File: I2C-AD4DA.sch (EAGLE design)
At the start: 11 parts, among them IC1 PCF8591T, X1 RJ45-FRONT

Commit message: 1.1
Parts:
- added CA, CB, CC, CD: 0.1uF, SPCoast:CAP0805
- added L1: 47 uH, rcl:L-USL2012C
- added U$1: AGND+DGND, SPCoast:AGND+DGND
- C1: device SPCoast-minimal:C-POL0810 -> SPCoast:CAP-POLUD10X10
- C2: device SPCoast-minimal:C0805 -> SPCoast:CAP0805
- I2C0, I2C1: value I2CLEFT -> CONNECTOR-I2CLEFT; device SPCoast-minimal:I2CLEFT -> SPCoast:CONNECTOR-I2CLEFT
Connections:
- new net N$1: IC1.VREF, L1.2
- net 5V: now also L1.1
- net AD0: now also CA.1
- net AD1: now also CB.1
- net AD2: now also CC.1
- net AD3: now also CD.1
- net AGND: now also CA.2, CB.2, CC.2, CD.2, IC1.AGND, U$1.P$1
- net GND: now also U$1.P$2; no longer IC1.AGND
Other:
- note added: "1.1"
- note removed: "1.0"
- moved on the sheet: A0, A1, A2, I2C0, I2C1, X1

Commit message: 2.0
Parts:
- removed U$9: BOARD50X50, SPCoast-minimal:BOARD50X50
- added BOARD1: (no value), SPCoast:BOARD80X50
- added CON1, CON2: CONNECTOR-GROVE-4P-2.0-3470130P1, SPCoast:CONNECTOR-GROVE-4P-2.0-3470130P1
- A0, A1, A2: device SPCoast-minimal:JUMPER-3-DEFAULT2.54MM -> SPCoast:JUMPER-3-DEFAULT2.54MM
- IC1: device micro-philips:PCF8591T -> SPCoast:PCF8591T
- L1: device rcl:L-USL2012C -> SPCoast:L-USL2012C
- LOGO1: value OSHW-LOGOL -> DOC-OSHW-LOGO-L; device SPCoast-minimal:OSHW-LOGOL -> SPCoast:DOC-OSHW-LOGO-L
- X1: value RJ45-FRONT -> (none); device SPCoast-minimal:RJ45-FRONT -> SPCoast:CONNECTOR-RJ45-FRONT
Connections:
- new net VIN: CON1.3, CON1.4, CON2.3, CON2.4
- net GND: now also CON1.1, CON1.2, CON2.1, CON2.2
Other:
- note added: "2.0"
- note removed: "1.1"

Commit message: 3.0
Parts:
- removed X1: (no value), SPCoast:CONNECTOR-RJ45-FRONT
- added C3, C4: 0.1uF, SPCoast:CAP0805
- added U$2, U$3, U$4, U$7: R-SLIDE-POT-45MM, SPCoast:R-SLIDE-POT-45MM
- A0, A1, A2: device SPCoast:JUMPER-3-DEFAULT2.54MM -> SPCoast:JUMPER-31-2
- BOARD1: device SPCoast:BOARD80X50 -> SPCoast:BOARD80X100
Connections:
- net 5V: now also C3.1, C4.1, U$2P1.E, U$3P1.E, U$4P1.E, U$7P1.E; no longer X1.1
- net AD0: now also U$7P1.S; no longer X1.2
- net AD1: now also U$4P1.S; no longer X1.3
- net AD2: now also U$3P1.S; no longer X1.4
- net AD3: now also U$2P1.S; no longer X1.5
- net AGND: now also C3.2, U$2G$1.AGND, U$2P1.A, U$3G$1.AGND, U$3P1.A, U$4G$1.AGND, U$4P1.A, U$7G$1.AGND, U$7P1.A; no longer X1.6
- net DA0: no longer X1.7
- net GND: now also C4.2; no longer X1.8
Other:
- note added: "1.0"
- note added: "3.0"
- note added: "4x slider pots for controlling light strips"
- note added: "D"
- note added: "Update: Fixed library footprint for sliders removed extra caps analog output to a pin set, not LED"
- note removed: "2.0"

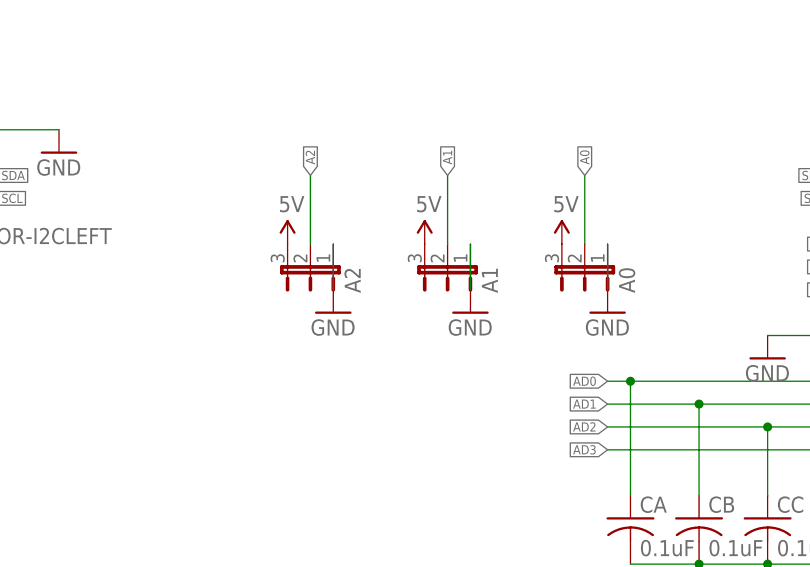
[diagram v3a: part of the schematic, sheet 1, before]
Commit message: added values for connectors
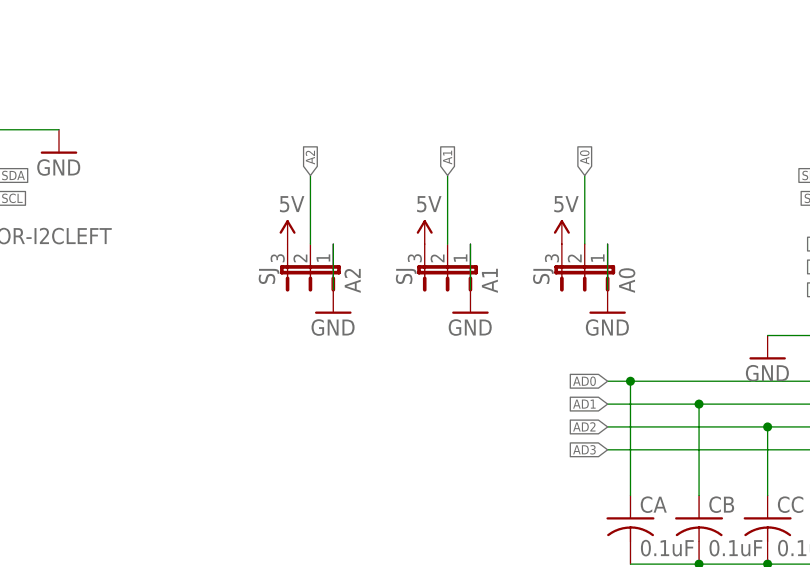
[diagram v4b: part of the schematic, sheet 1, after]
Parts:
- A0, A1, A2: value (none) -> SJ
- BOARD1: value (none) -> 10x10
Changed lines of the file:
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@@
 <part name="GND1" library="SparkFun-Aesthetics" deviceset="GND" device=""/>
 <part name="GND6" library="SparkFun-Aesthetics" deviceset="GND" device=""/>
-<part name="A2" library="SPCoast" deviceset="JUMPER-3" device="1-2"/>
-<part name="A1" library="SPCoast" deviceset="JUMPER-3" device="1-2"/>
-<part name="A0" library="SPCoast" deviceset="JUMPER-3" device="1-2"/>
+<part name="A2" library="SPCoast" deviceset="JUMPER-3" device="1-2" value="SJ"/>
+<part name="A1" library="SPCoast" deviceset="JUMPER-3" device="1-2" value="SJ"/>
+<part name="A0" library="SPCoast" deviceset="JUMPER-3" device="1-2" value="SJ"/>
 <part name="GND7" library="SparkFun-Aesthetics" deviceset="GND" device=""/>
 <part name="L1" library="SPCoast" deviceset="L-US" device="L2012C" value="47 uH"/>
@@
 <part name="U$1" library="SPCoast" deviceset="AGND+DGND" device=""/>
 <part name="GND4" library="SparkFun-Aesthetics" deviceset="GND" device=""/>
-<part name="BOARD1" library="SPCoast" deviceset="BOARD" device="80X100"/>
+<part name="BOARD1" library="SPCoast" deviceset="BOARD" device="80X100" value="10x10"/>
 <part name="CON1" library="SPCoast" deviceset="CONNECTOR-GROVE-4P-2.0" device="-3470130P1"/>
 <part name="CON2" library="SPCoast" deviceset="CONNECTOR-GROVE-4P-2.0" device="-3470130P1"/>

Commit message: normalized values
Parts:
- BOARD1: value 10x10 -> BOARD
- C1: value 150uF -> 220uF; device SPCoast:CAP-POLUD10X10 -> SPCoast:CAP-POL0810
- CON1, CON2: value CONNECTOR-GROVE-4P-2.0-3470130P1 -> 2mm
- I2C0, I2C1: value CONNECTOR-I2CLEFT -> I2C
- LOGO1: value DOC-OSHW-LOGO-L -> OSHW
- U$3, U$4, U$7: value R-SLIDE-POT-45MM -> (none)
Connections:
- net 5V: now also U$2RS1.E, U$3RS1.E, U$4RS1.E, U$7RS1.E; no longer U$2P1.E, U$3P1.E, U$4P1.E, U$7P1.E
- net AD0: now also U$7RS1.S; no longer U$7P1.S
- net AD1: now also U$4RS1.S; no longer U$4P1.S
- net AD2: now also U$3RS1.S; no longer U$3P1.S
- net AD3: now also U$2RS1.S; no longer U$2P1.S
- net AGND: now also U$2G1.AGND, U$2RS1.A, U$3G1.AGND, U$3RS1.A, U$4G1.AGND, U$4RS1.A, U$7G1.AGND, U$7RS1.A; no longer U$2G$1.AGND, U$2P1.A, U$3G$1.AGND, U$3P1.A, U$4G$1.AGND, U$4P1.A, U$7G$1.AGND, U$7P1.A
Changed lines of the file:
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@@
 <part name="GND3" library="SparkFun-Aesthetics" deviceset="GND" device=""/>
 <part name="SUPPLY1" library="SparkFun-Aesthetics" deviceset="5V" device=""/>
-<part name="C1" library="SPCoast" deviceset="CAP-POL*" device="UD10X10" value="150uF"/>
+<part name="C1" library="SPCoast" deviceset="CAP-POL*" device="0810" value="220uF"/>
 <part name="SUPPLY13" library="SparkFun-Aesthetics" deviceset="5V" device=""/>
 <part name="GND15" library="SparkFun-Aesthetics" deviceset="GND" device=""/>
 <part name="IC1" library="SPCoast" deviceset="PCF8591" device="T"/>
-<part name="I2C1" library="SPCoast" deviceset="CONNECTOR-I2C" device="LEFT"/>
-<part name="I2C0" library="SPCoast" deviceset="CONNECTOR-I2C" device="LEFT"/>
+<part name="I2C1" library="SPCoast" deviceset="CONNECTOR-I2C" device="LEFT" value="I2C"/>
+<part name="I2C0" library="SPCoast" deviceset="CONNECTOR-I2C" device="LEFT" value="I2C"/>
 <part name="SUPPLY2" library="SparkFun-Aesthetics" deviceset="5V" device=""/>
 <part name="GND1" library="SparkFun-Aesthetics" deviceset="GND" device=""/>
@@
 <part name="GND7" library="SparkFun-Aesthetics" deviceset="GND" device=""/>
 <part name="L1" library="SPCoast" deviceset="L-US" device="L2012C" value="47 uH"/>
-<part name="LOGO1" library="SPCoast" deviceset="DOC-OSHW-LOGO-" device="L" value="DOC-OSHW-LOGO-L"/>
+<part name="LOGO1" library="SPCoast" deviceset="DOC-OSHW-LOGO-" device="L" value="OSHW"/>
 <part name="C2" library="SPCoast" deviceset="CAP*" device="0805" value="0.1uF"/>
 <part name="CC" library="SPCoast" deviceset="CAP*" device="0805" value="0.1uF"/>
@@
 <part name="U$1" library="SPCoast" deviceset="AGND+DGND" device=""/>
 <part name="GND4" library="SparkFun-Aesthetics" deviceset="GND" device=""/>
-<part name="BOARD1" library="SPCoast" deviceset="BOARD" device="80X100" value="10x10"/>
-<part name="CON1" library="SPCoast" deviceset="CONNECTOR-GROVE-4P-2.0" device="-3470130P1"/>
-<part name="CON2" library="SPCoast" deviceset="CONNECTOR-GROVE-4P-2.0" device="-3470130P1"/>
+<part name="BOARD1" library="SPCoast" deviceset="BOARD" device="80X100" value="BOARD"/>
+<part name="CON1" library="SPCoast" deviceset="CONNECTOR-GROVE-4P-2.0" device="-3470130P1" value="2mm"/>
+<part name="CON2" library="SPCoast" deviceset="CONNECTOR-GROVE-4P-2.0" device="-3470130P1" value="2mm"/>
 <part name="GND8" library="SparkFun-Aesthetics" deviceset="GND" device=""/>
 <part name="FRAME2" library="SPCoast-minimal" deviceset="FRAME-LETTER" device=""/>
@@
 <instance part="GND1" gate="1" x="66.04" y="119.38"/>
 <instance part="GND6" gate="1" x="144.78" y="96.52"/>
-<instance part="A2" gate="G$1" x="96.52" y="106.68" rot="R180"/>
-<instance part="A1" gate="G$1" x="111.76" y="106.68" rot="R180"/>
-<instance part="A0" gate="G$1" x="127" y="106.68" rot="R180"/>
+<instance part="A2" gate="J" x="96.52" y="106.68" rot="R180"/>
+<instance part="A1" gate="J" x="111.76" y="106.68" rot="R180"/>
+<instance part="A0" gate="J" x="127" y="106.68" rot="R180"/>
 <instance part="GND7" gate="1" x="96.52" y="101.6"/>
 <instance part="L1" gate="G$1" x="180.34" y="111.76"/>
@@
 <instance part="U$1" gate="G$1" x="165.1" y="73.66"/>
 <instance part="GND4" gate="1" x="170.18" y="71.12"/>
-<instance part="BOARD1" gate="G$1" x="238.76" y="33.02"/>
+<instance part="BOARD1" gate="B" x="238.76" y="33.02"/>
 <instance part="CON1" gate="J" x="33.02" y="147.32"/>
 <instance part="CON2" gate="J" x="48.26" y="147.32" rot="MR0"/>
@@
 <wire x1="124.46" y1="109.22" x2="124.46" y2="116.84" width="0.1524" layer="91"/>
 <label x="124.46" y="116.84" size="1.016" layer="95" rot="R90" xref="yes"/>
-<pinref part="A0" gate="G$1" pin="2"/>
+<pinref part="A0" gate="J" pin="2"/>
 </segment>
 </net>
@@
 <wire x1="109.22" y1="109.22" x2="109.22" y2="116.84" width="0.1524" layer="91"/>
 <label x="109.22" y="116.84" size="1.016" layer="95" rot="R90" xref="yes"/>
-<pinref part="A1" gate="G$1" pin="2"/>
+<pinref part="A1" gate="J" pin="2"/>
 </segment>
 </net>
@@
 <wire x1="93.98" y1="109.22" x2="93.98" y2="116.84" width="0.1524" layer="91"/>
 <label x="93.98" y="116.84" size="1.016" layer="95" rot="R90" xref="yes"/>
-<pinref part="A2" gate="G$1" pin="2"/>
+<pinref part="A2" gate="J" pin="2"/>
 </segment>
 </net>
@@
 </segment>
 <segment>
-<pinref part="A2" gate="G$1" pin="3"/>
+<pinref part="A2" gate="J" pin="3"/>
 <pinref part="SUPPLY7" gate="G$1" pin="5V"/>
 </segment>
 <segment>
-<pinref part="A1" gate="G$1" pin="3"/>
+<pinref part="A1" gate="J" pin="3"/>
 <pinref part="SUPPLY11" gate="G$1" pin="5V"/>
 </segment>
 <segment>
-<pinref part="A0" gate="G$1" pin="3"/>
+<pinref part="A0" gate="J" pin="3"/>
 <pinref part="SUPPLY12" gate="G$1" pin="5V"/>
 </segment>
@@
 </segment>
 <segment>
-<pinref part="A2" gate="G$1" pin="1"/>
+<pinref part="A2" gate="J" pin="1"/>
 <pinref part="GND7" gate="1" pin="GND"/>
 <wire x1="96.52" y1="104.14" x2="96.52" y2="109.22" width="0.1524" layer="91"/>
@@
 <pinref part="GND9" gate="1" pin="GND"/>
 <wire x1="111.76" y1="109.22" x2="111.76" y2="104.14" width="0.1524" layer="91"/>
-<pinref part="A1" gate="G$1" pin="1"/>
-</segment>
-<segment>
-<pinref part="A0" gate="G$1" pin="1"/>
+<pinref part="A1" gate="J" pin="1"/>
+</segment>
+<segment>
+<pinref part="A0" gate="J" pin="1"/>
 <pinref part="GND10" gate="1" pin="GND"/>
 <wire x1="127" y1="109.22" x2="127" y2="104.14" width="0.1524" layer="91"/>
@@
 <instance part="FRAME2" gate="FRAME" x="0" y="0"/>
 <instance part="FRAME2" gate="FRAME_CONTENT" x="147.32" y="0"/>
-<instance part="U$2" gate="P1" x="33.02" y="134.62"/>
-<instance part="U$3" gate="P1" x="50.8" y="134.62"/>
-<instance part="U$4" gate="P1" x="68.58" y="134.62"/>
-<instance part="U$7" gate="P1" x="99.06" y="134.62"/>
+<instance part="U$2" gate="RS1" x="33.02" y="134.62"/>
+<instance part="U$3" gate="RS1" x="50.8" y="134.62"/>
+<instance part="U$4" gate="RS1" x="68.58" y="134.62"/>
+<instance part="U$7" gate="RS1" x="99.06" y="134.62"/>
 <instance part="SUPPLY4" gate="G$1" x="99.06" y="142.24"/>
 <instance part="SUPPLY8" gate="G$1" x="68.58" y="142.24"/>
@@
 <instance part="C4" gate="C1" x="139.7" y="132.08"/>
 <instance part="GND5" gate="1" x="139.7" y="124.46"/>
-<instance part="U$2" gate="G$1" x="33.02" y="124.46"/>
-<instance part="U$3" gate="G$1" x="50.8" y="124.46"/>
-<instance part="U$4" gate="G$1" x="68.58" y="124.46"/>
-<instance part="U$7" gate="G$1" x="119.38" y="124.46"/>
+<instance part="U$2" gate="G1" x="33.02" y="124.46"/>
+<instance part="U$3" gate="G1" x="50.8" y="124.46"/>
+<instance part="U$4" gate="G1" x="68.58" y="124.46"/>
+<instance part="U$7" gate="G1" x="119.38" y="124.46"/>
 </instances>
 <busses>
@@
 <net name="5V" class="0">
 <segment>
-<pinref part="U$7" gate="P1" pin="E"/>
+<pinref part="U$7" gate="RS1" pin="E"/>
 <pinref part="SUPPLY4" gate="G$1" pin="5V"/>
 </segment>
 <segment>
-<pinref part="U$4" gate="P1" pin="E"/>
+<pinref part="U$4" gate="RS1" pin="E"/>
 <pinref part="SUPPLY8" gate="G$1" pin="5V"/>
 </segment>
 <segment>
-<pinref part="U$3" gate="P1" pin="E"/>
+<pinref part="U$3" gate="RS1" pin="E"/>
 <pinref part="SUPPLY9" gate="G$1" pin="5V"/>
 </segment>
 <segment>
-<pinref part="U$2" gate="P1" pin="E"/>
+<pinref part="U$2" gate="RS1" pin="E"/>
 <pinref part="SUPPLY10" gate="G$1" pin="5V"/>
 </segment>
@@
 <net name="AD0" class="0">
 <segment>
-<pinref part="U$7" gate="P1" pin="S"/>
+<pinref part="U$7" gate="RS1" pin="S"/>
 <wire x1="104.14" y1="134.62" x2="106.68" y2="134.62" width="0.1524" layer="91"/>
 <label x="106.68" y="134.62" size="1.016" layer="95" xref="yes"/>
@@
 <net name="AD1" class="0">
 <segment>
-<pinref part="U$4" gate="P1" pin="S"/>
+<pinref part="U$4" gate="RS1" pin="S"/>
 <wire x1="73.66" y1="134.62" x2="76.2" y2="134.62" width="0.1524" layer="91"/>
 <label x="76.2" y="134.62" size="1.016" layer="95" xref="yes"/>
@@
 <net name="AD2" class="0">
 <segment>
-<pinref part="U$3" gate="P1" pin="S"/>
+<pinref part="U$3" gate="RS1" pin="S"/>
 <wire x1="55.88" y1="134.62" x2="58.42" y2="134.62" width="0.1524" layer="91"/>
 <label x="58.42" y="134.62" size="1.016" layer="95" xref="yes"/>
@@
 <net name="AD3" class="0">
 <segment>
-<pinref part="U$2" gate="P1" pin="S"/>
+<pinref part="U$2" gate="RS1" pin="S"/>
 <wire x1="38.1" y1="134.62" x2="40.64" y2="134.62" width="0.1524" layer="91"/>
 <label x="40.64" y="134.62" size="1.016" layer="95" xref="yes"/>
@@
 <net name="AGND" class="0">
 <segment>
-<pinref part="U$2" gate="P1" pin="A"/>
-<pinref part="U$3" gate="P1" pin="A"/>
+<pinref part="U$2" gate="RS1" pin="A"/>
+<pinref part="U$3" gate="RS1" pin="A"/>
 <wire x1="33.02" y1="127" x2="50.8" y2="127" width="0.1524" layer="91"/>
-<pinref part="U$4" gate="P1" pin="A"/>
+<pinref part="U$4" gate="RS1" pin="A"/>
 <wire x1="50.8" y1="127" x2="68.58" y2="127" width="0.1524" layer="91"/>
 <junction x="50.8" y="127"/>
-<pinref part="U$7" gate="P1" pin="A"/>
+<pinref part="U$7" gate="RS1" pin="A"/>
 <wire x1="68.58" y1="127" x2="99.06" y2="127" width="0.1524" layer="91"/>
 <junction x="68.58" y="127"/>
@@
 <junction x="119.38" y="127"/>
 <wire x1="119.38" y1="127" x2="114.3" y2="127" width="0.1524" layer="91"/>
-<pinref part="U$2" gate="G$1" pin="AGND"/>
+<pinref part="U$2" gate="G1" pin="AGND"/>
 <junction x="33.02" y="127"/>
-<pinref part="U$3" gate="G$1" pin="AGND"/>
-<pinref part="U$4" gate="G$1" pin="AGND"/>
-<pinref part="U$7" gate="G$1" pin="AGND"/>
-</segment>
-</net>
+<pinref part="U$3" gate="G1" pin="AGND"/>
+<pinref part="U$4" gate="G1" pin="AGND"/>
+<pinref part="U$7" gate="G1" pin="AGND"/>
+</segment>
+</net>

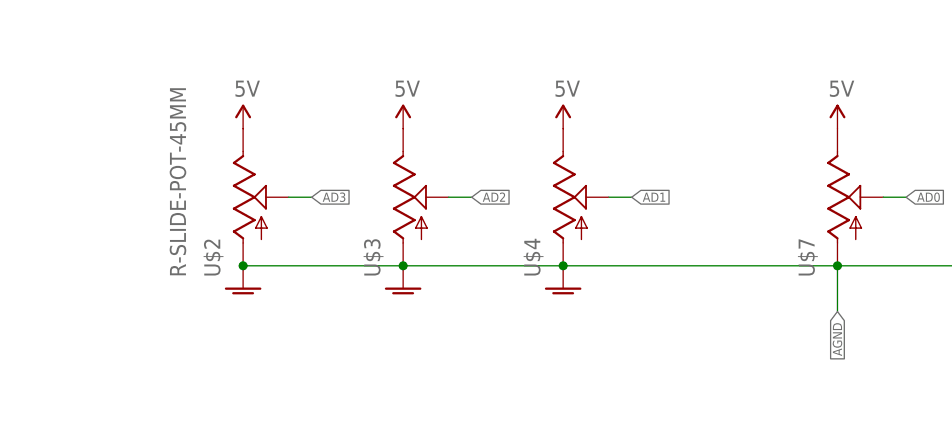
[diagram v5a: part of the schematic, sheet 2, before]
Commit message: normalized values
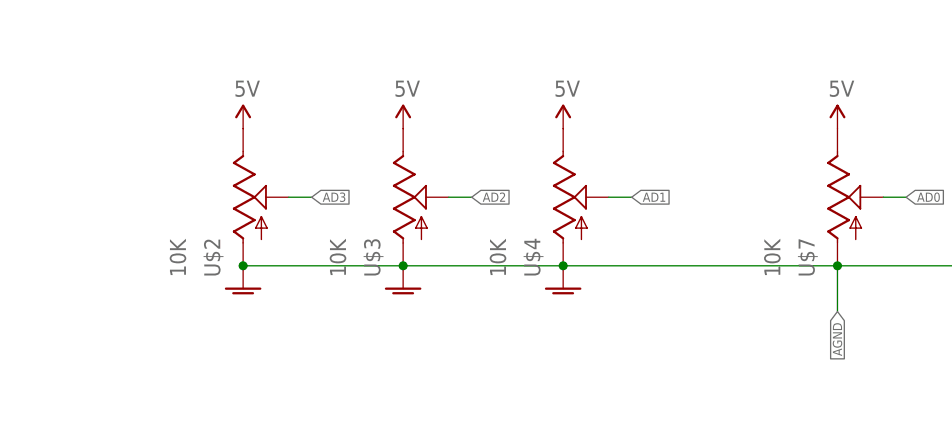
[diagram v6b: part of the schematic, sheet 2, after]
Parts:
- U$2: value R-SLIDE-POT-45MM -> 10K
- U$3, U$4, U$7: value (none) -> 10K
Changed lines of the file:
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@@
 <part name="GND8" library="SparkFun-Aesthetics" deviceset="GND" device=""/>
 <part name="FRAME2" library="SPCoast-minimal" deviceset="FRAME-LETTER" device=""/>
-<part name="U$2" library="SPCoast" deviceset="R-SLIDE-POT" device="-45MM" value="R-SLIDE-POT-45MM"/>
-<part name="U$3" library="SPCoast" deviceset="R-SLIDE-POT" device="-45MM"/>
-<part name="U$4" library="SPCoast" deviceset="R-SLIDE-POT" device="-45MM"/>
-<part name="U$7" library="SPCoast" deviceset="R-SLIDE-POT" device="-45MM"/>
+<part name="U$2" library="SPCoast" deviceset="R-SLIDE-POT" device="-45MM" value="10K"/>
+<part name="U$3" library="SPCoast" deviceset="R-SLIDE-POT" device="-45MM" value="10K"/>
+<part name="U$4" library="SPCoast" deviceset="R-SLIDE-POT" device="-45MM" value="10K"/>
+<part name="U$7" library="SPCoast" deviceset="R-SLIDE-POT" device="-45MM" value="10K"/>
 <part name="SUPPLY4" library="SparkFun-Aesthetics" deviceset="5V" device=""/>
 <part name="SUPPLY8" library="SparkFun-Aesthetics" deviceset="5V" device=""/>
